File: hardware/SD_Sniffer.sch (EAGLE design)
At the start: 10 parts, among them U1 SD_CARD_SOCKET4UCON, U2 SD_MMC_CARDSD_PCB

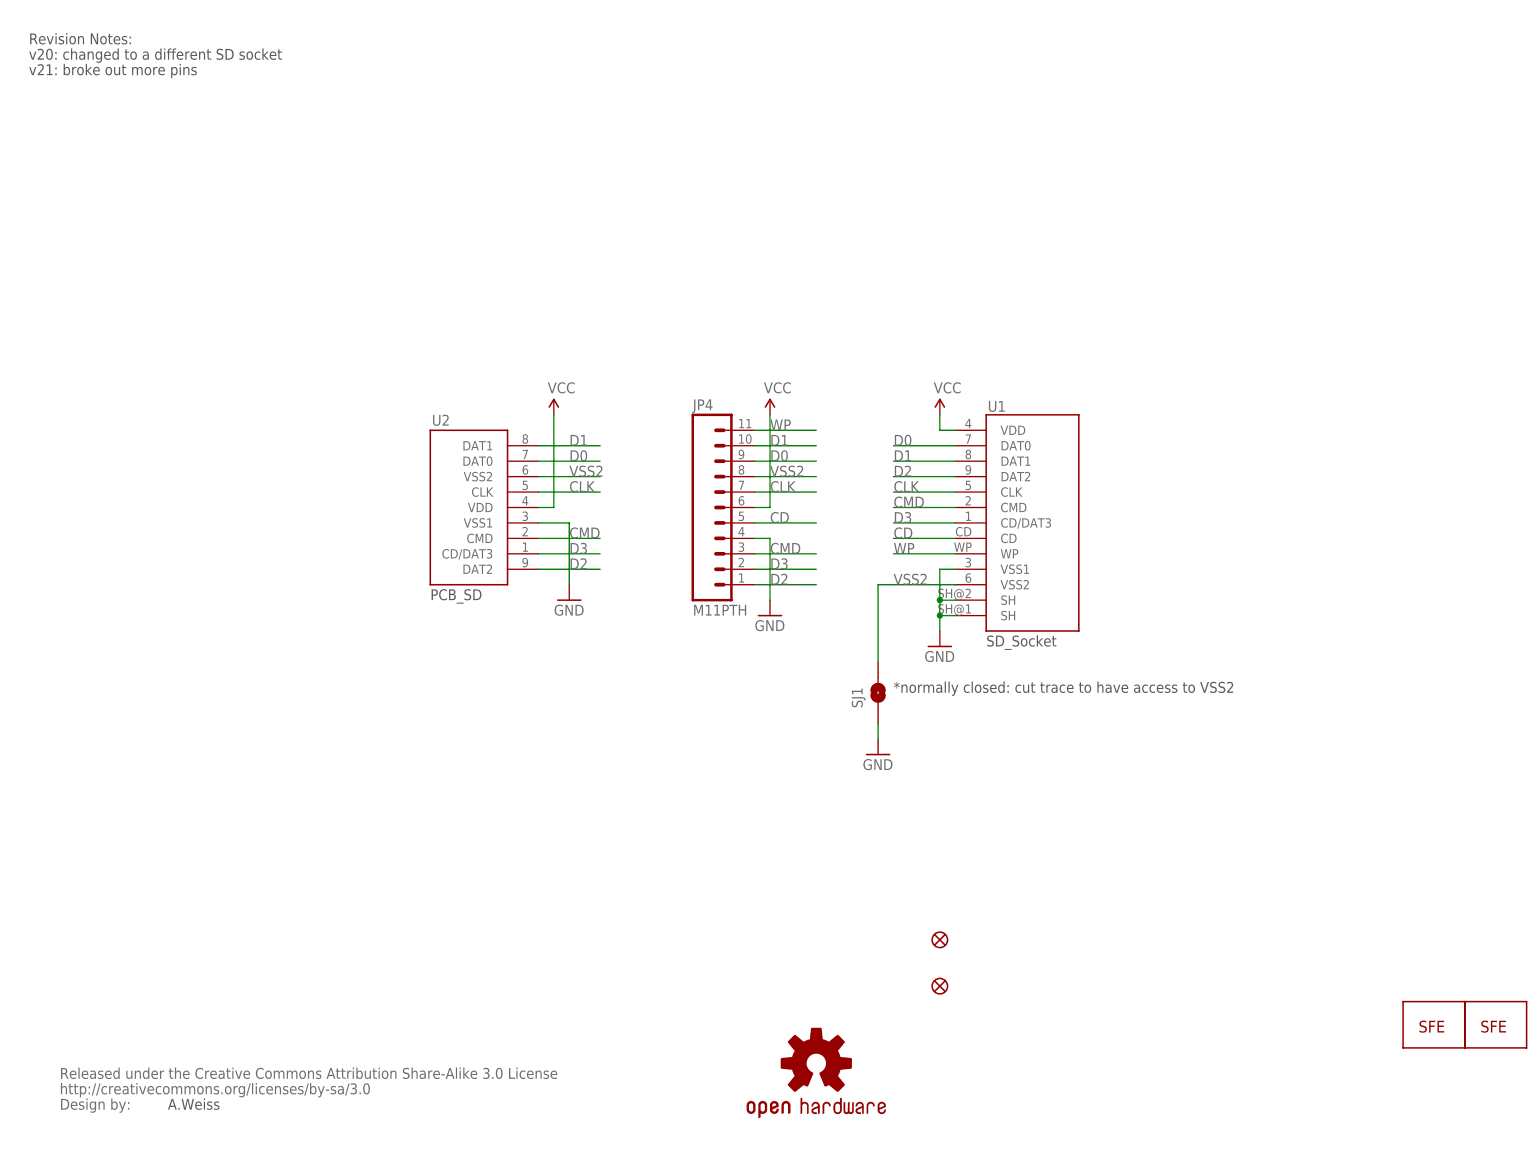
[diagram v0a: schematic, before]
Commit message: Moved via, Added Bigger Flame, Named Jumper
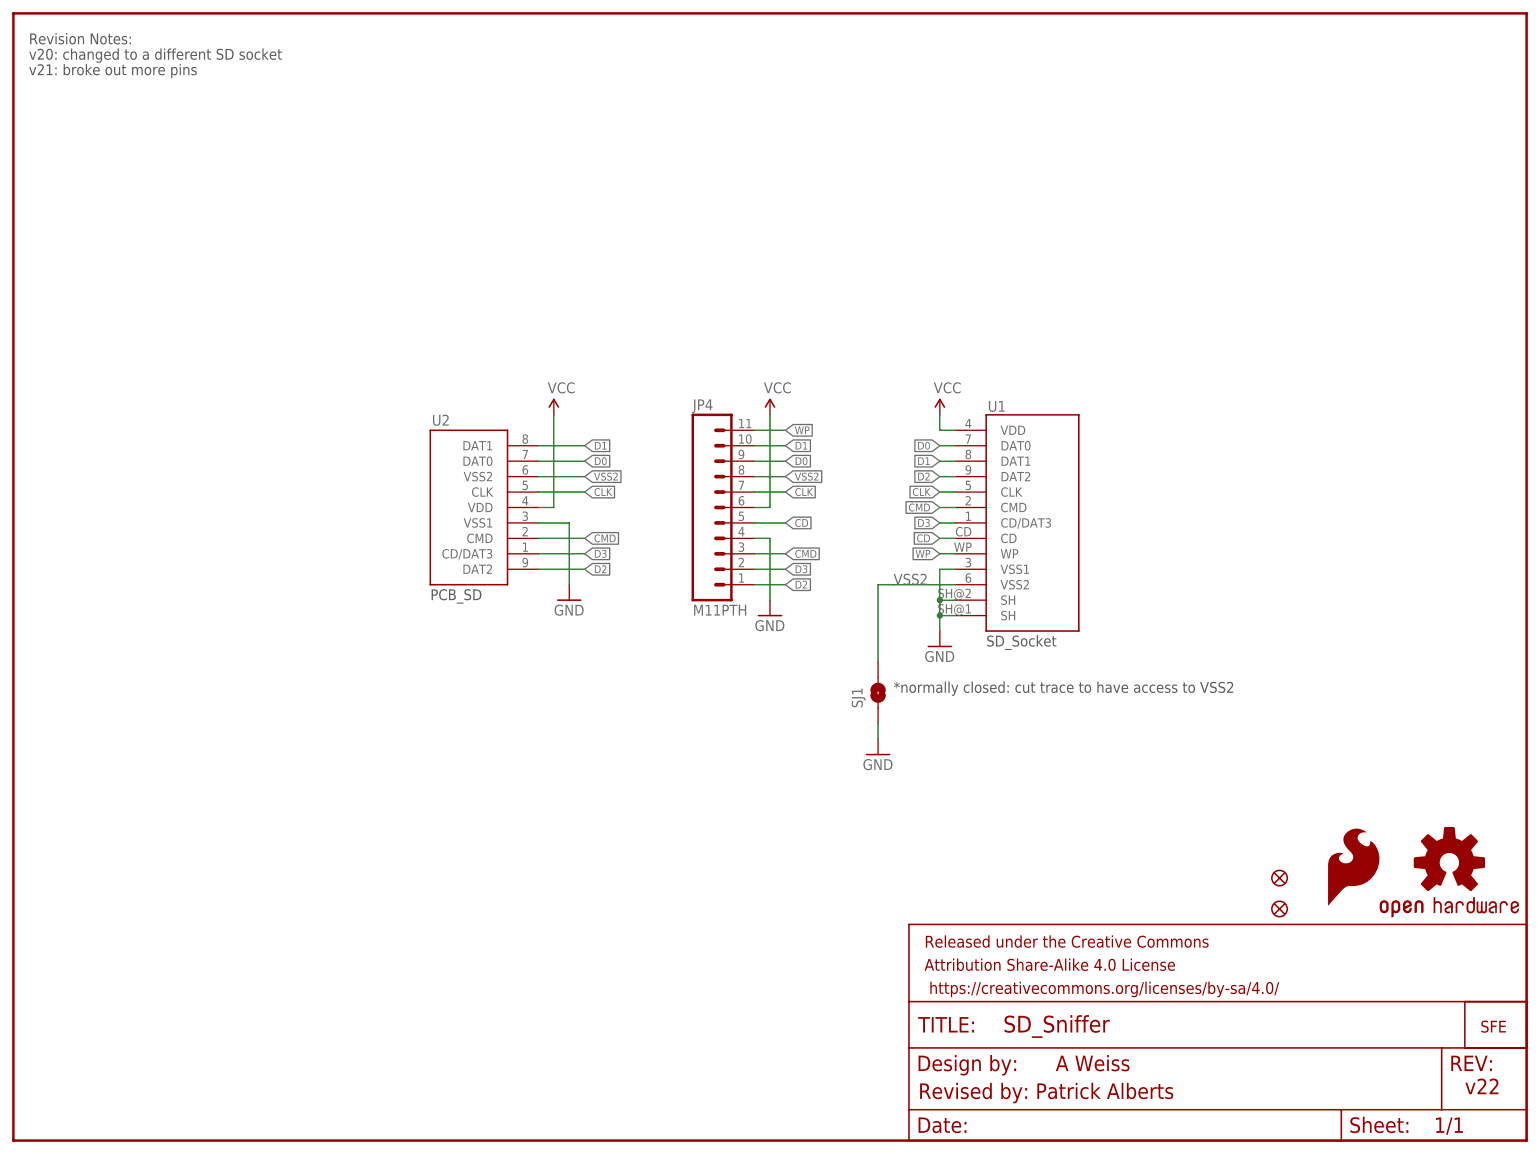
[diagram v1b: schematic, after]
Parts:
- removed U$1: CREATIVE_COMMONS, SparkFun-Aesthetics:CREATIVE_COMMONS
- added FRAME1: FRAME-LETTER, SparkFun-Aesthetics:FRAME-LETTER
- U$4: value LOGO-SFESK -> SFE_LOGO_FLAME.2_INCH; device SparkFun:LOGO-SFESK -> SparkFun-Aesthetics:SFE_LOGO_FLAME.2_INCH
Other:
- note added: "A Weiss"
- note added: "Revised by: Patrick Alberts"
- note added: "v22"
- note removed: "A.Weiss"

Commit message: Added updated SD socket
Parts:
- U1: value SD_CARD_SOCKET4UCON -> SD_CARD_SOCKET; device SparkFun-Connectors:SD_CARD_SOCKET4UCON -> SparkFun-Connectors:SD_CARD_SOCKET
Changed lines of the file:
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@@
 <part name="LOGO" library="SparkFun" deviceset="LOGO-SFE" device="NEW"/>
 <part name="U$4" library="SparkFun-Aesthetics" deviceset="SFE_LOGO_FLAME" device=".2_INCH" value="SFE_LOGO_FLAME.2_INCH"/>
-<part name="U1" library="SparkFun-Connectors" deviceset="SD_CARD_SOCKET" device="4UCON"/>
+<part name="U1" library="SparkFun-Connectors" deviceset="SD_CARD_SOCKET" device="" value="SD_CARD_SOCKET"/>
 <part name="GND1" library="SparkFun-Aesthetics" deviceset="GND" device=""/>
 <part name="P+1" library="SparkFun-Aesthetics" deviceset="VCC" device=""/>

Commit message: Fixed eagle sync
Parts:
- U2: device SparkFun:SD_MMC_CARDSD_PCB -> SparkFun-Boards:SD_MMC_CARDSD_PCB
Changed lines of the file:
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@@
 </classes>
 <parts>
-<part name="U2" library="SparkFun" deviceset="SD_MMC_CARD" device="SD_PCB"/>
+<part name="U2" library="SparkFun-Boards" deviceset="SD_MMC_CARD" device="SD_PCB"/>
 <part name="FRAME1" library="SparkFun-Aesthetics" deviceset="FRAME-LETTER" device=""/>
 <part name="LOGO" library="SparkFun" deviceset="LOGO-SFE" device="NEW"/>
